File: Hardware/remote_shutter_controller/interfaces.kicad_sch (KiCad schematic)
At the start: 5 parts

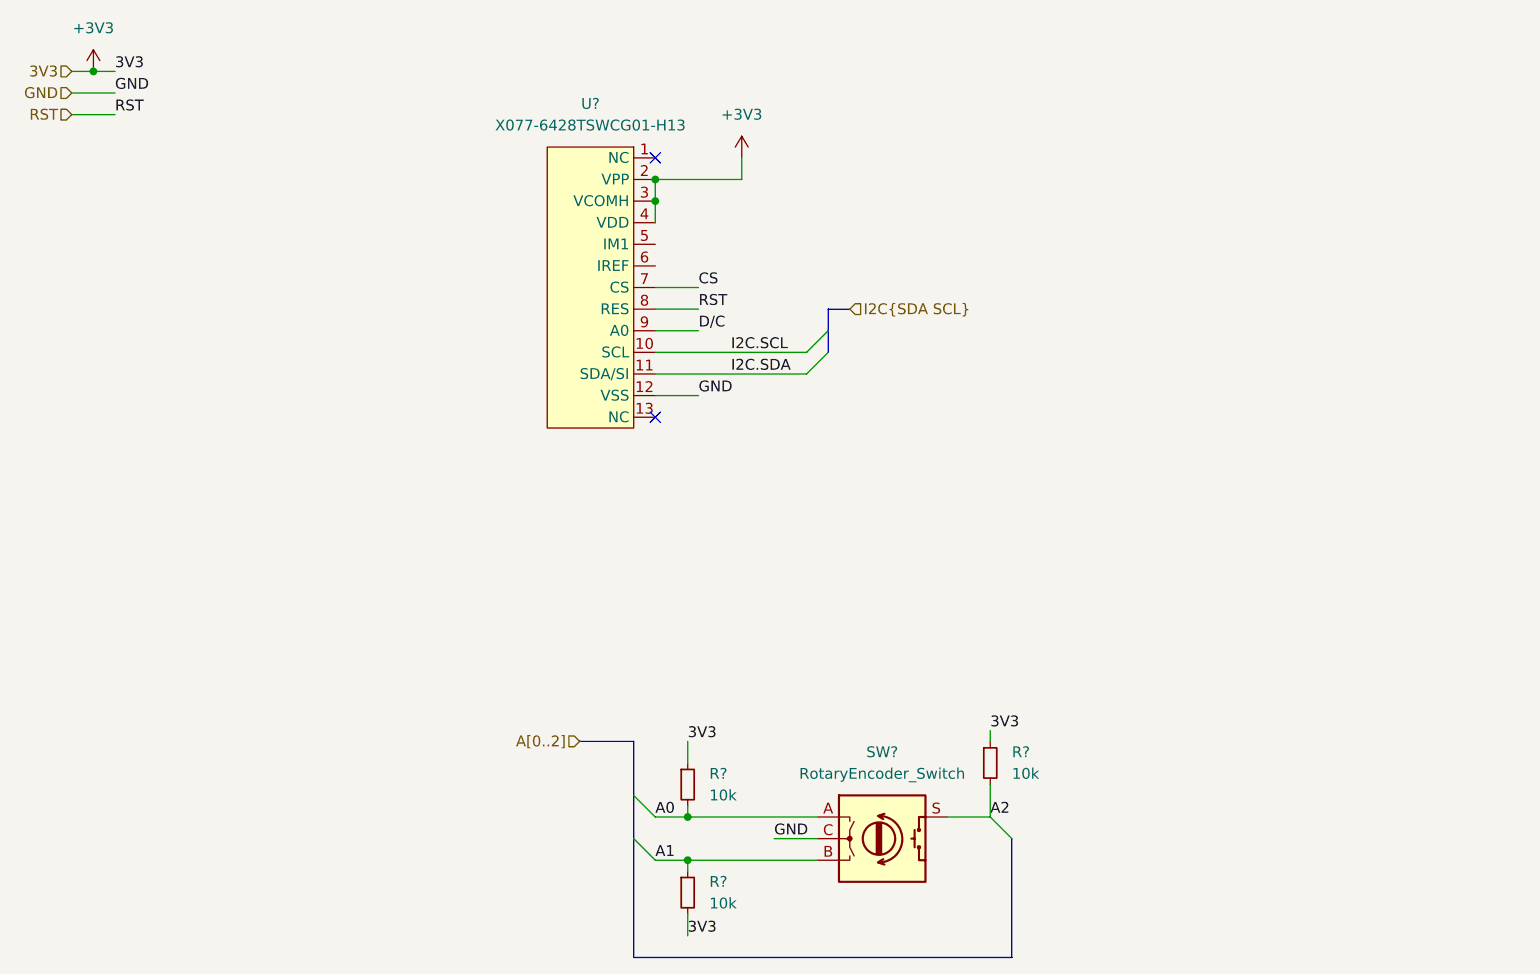
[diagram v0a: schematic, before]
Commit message: Schematic updates. First export to PCB
Added 9V line, OLED switch circuit. Added OLED footprint.
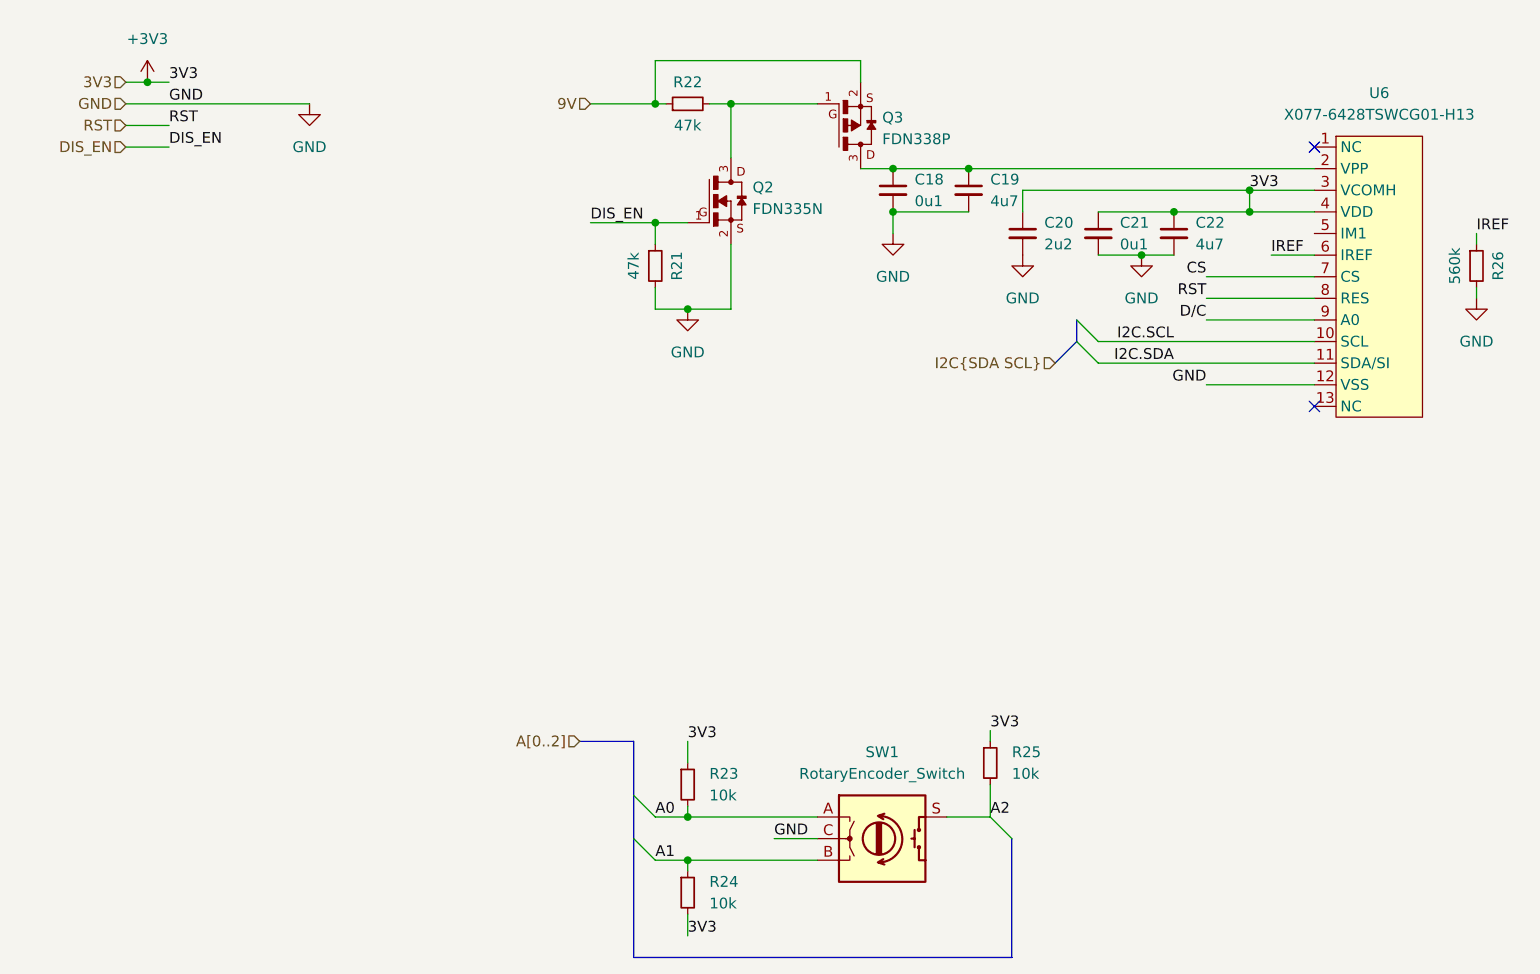
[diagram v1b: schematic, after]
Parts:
- added C18, C21: 0u1, Capacitor_SMD:C_0603_1608Metric_Pad1.08x0.95mm_HandSolder, symbol Device:C_Small
- added C19, C22: 4u7, Capacitor_SMD:C_0603_1608Metric_Pad1.08x0.95mm_HandSolder, symbol Device:C_Small
- added C20: 2u2, Capacitor_SMD:C_0603_1608Metric_Pad1.08x0.95mm_HandSolder, symbol Device:C_Small
- added Q2: FDN335N, fpr:SSOT-3, symbol FDN335N:FDN335N
- added Q3: FDN338P, fpr:SSOT-3, symbol FDN338P:FDN338P
- added R21, R22: 47k, Resistor_SMD:R_0603_1608Metric_Pad0.98x0.95mm_HandSolder, symbol Device:R_Small
- added R26: 560k, Resistor_SMD:R_0603_1608Metric_Pad0.98x0.95mm_HandSolder, symbol Device:R_Small
- U6: renamed from U?; footprint (none) -> footprint:X077-6428TSWCG01-H13
- gave numbers to parts that had none: 4
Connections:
- net +3V3: now also C20.1, C21.1, C22.1; no longer U6.2 (VPP)
- net GND: now also C18.2, C19.2, C20.2, C21.2, C22.2, Q2.2, R21.2, R26.2
- net IREF: now reaches U6.6 (IREF)
- net IREF: now also R26.1
- new net: Q2.3, Q3.1, R22.2
- new net: C18.1, C19.1, Q3.3, U6.2 (VPP)
- new net 9V: Q3.2, R22.1
- new net DIS_EN: Q2.1, R21.1
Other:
- moved on the sheet: U6
